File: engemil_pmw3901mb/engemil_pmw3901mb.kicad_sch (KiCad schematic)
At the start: 18 parts, among them J1 6130XX11121, U1 PMW3901MB-TXQT, U2 TLV77333PDBVR, U3 TLV77318PDBVR

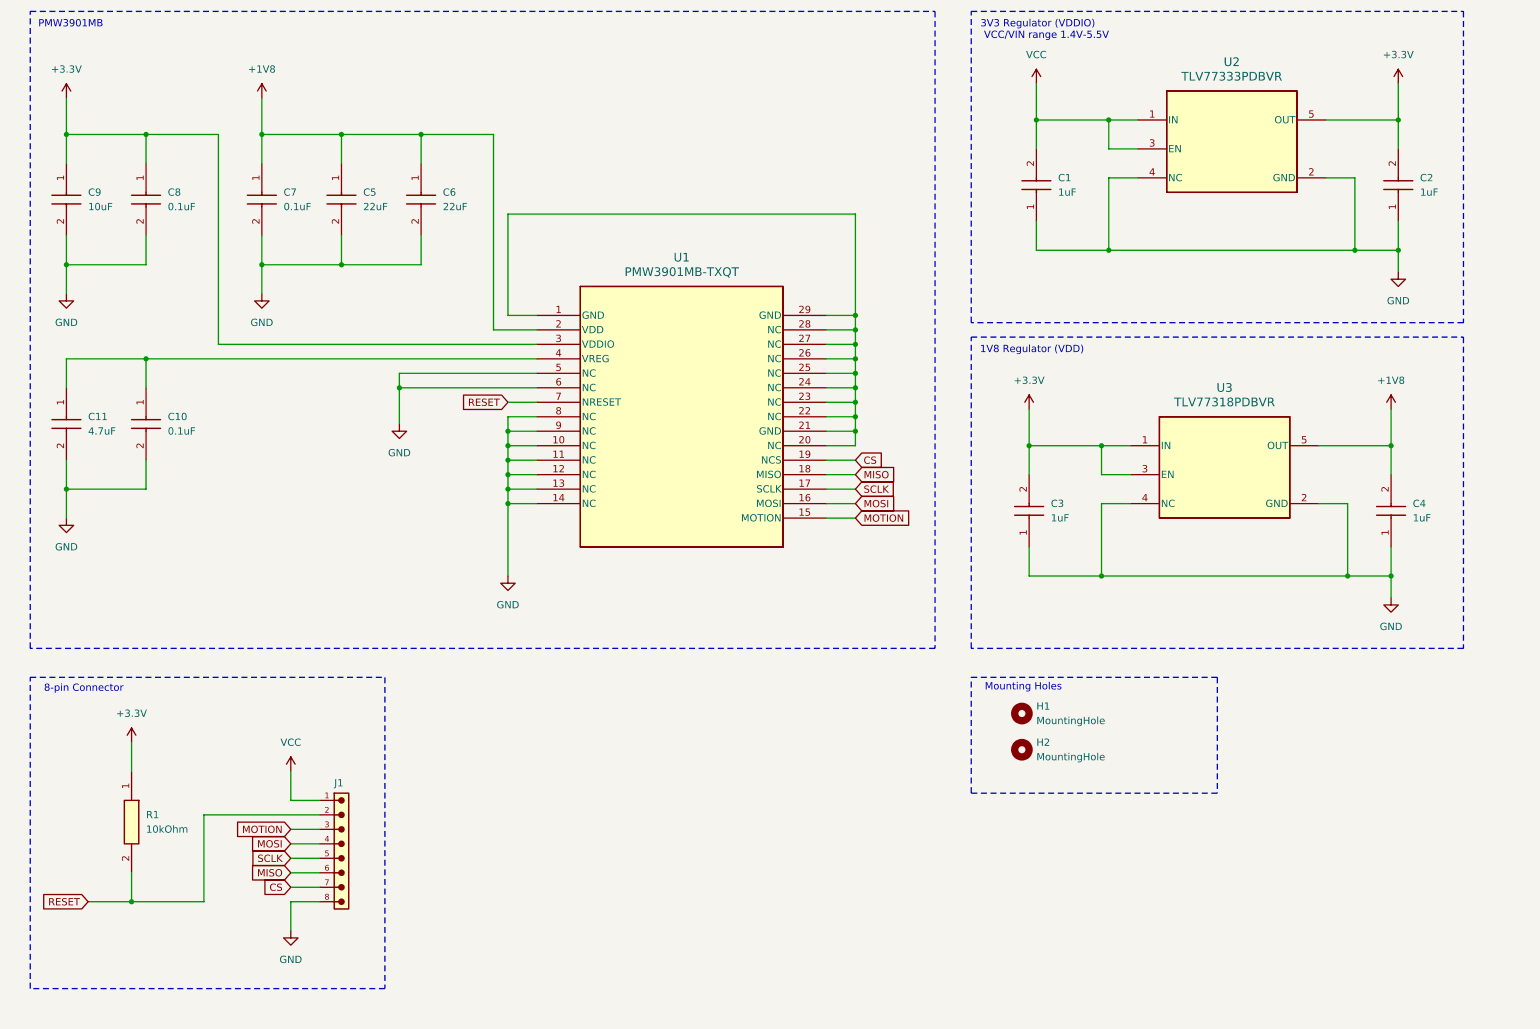
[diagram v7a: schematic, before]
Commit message: - Removed 3v3 voltage regulator and two capacitors - Changed reference designators (C1,C2,...,U2,U3,...) - Added R4 - Marked C3 and C4 as not mount - Added comment about RC filter - Added pull-up resistors for SCLK and MISO - Marked R2 and R3 as not mount - Added notes for 8-pin connector - Added ESD protection diodes - Updated BOM - Removed zip file in raw folder (unused and not imported) - Added datasheets for components under docs folder - Imported new components into project - Updated schematic version and date - Generated new schematic pdf - Started on redesigning pcb layout (work-in-progress)
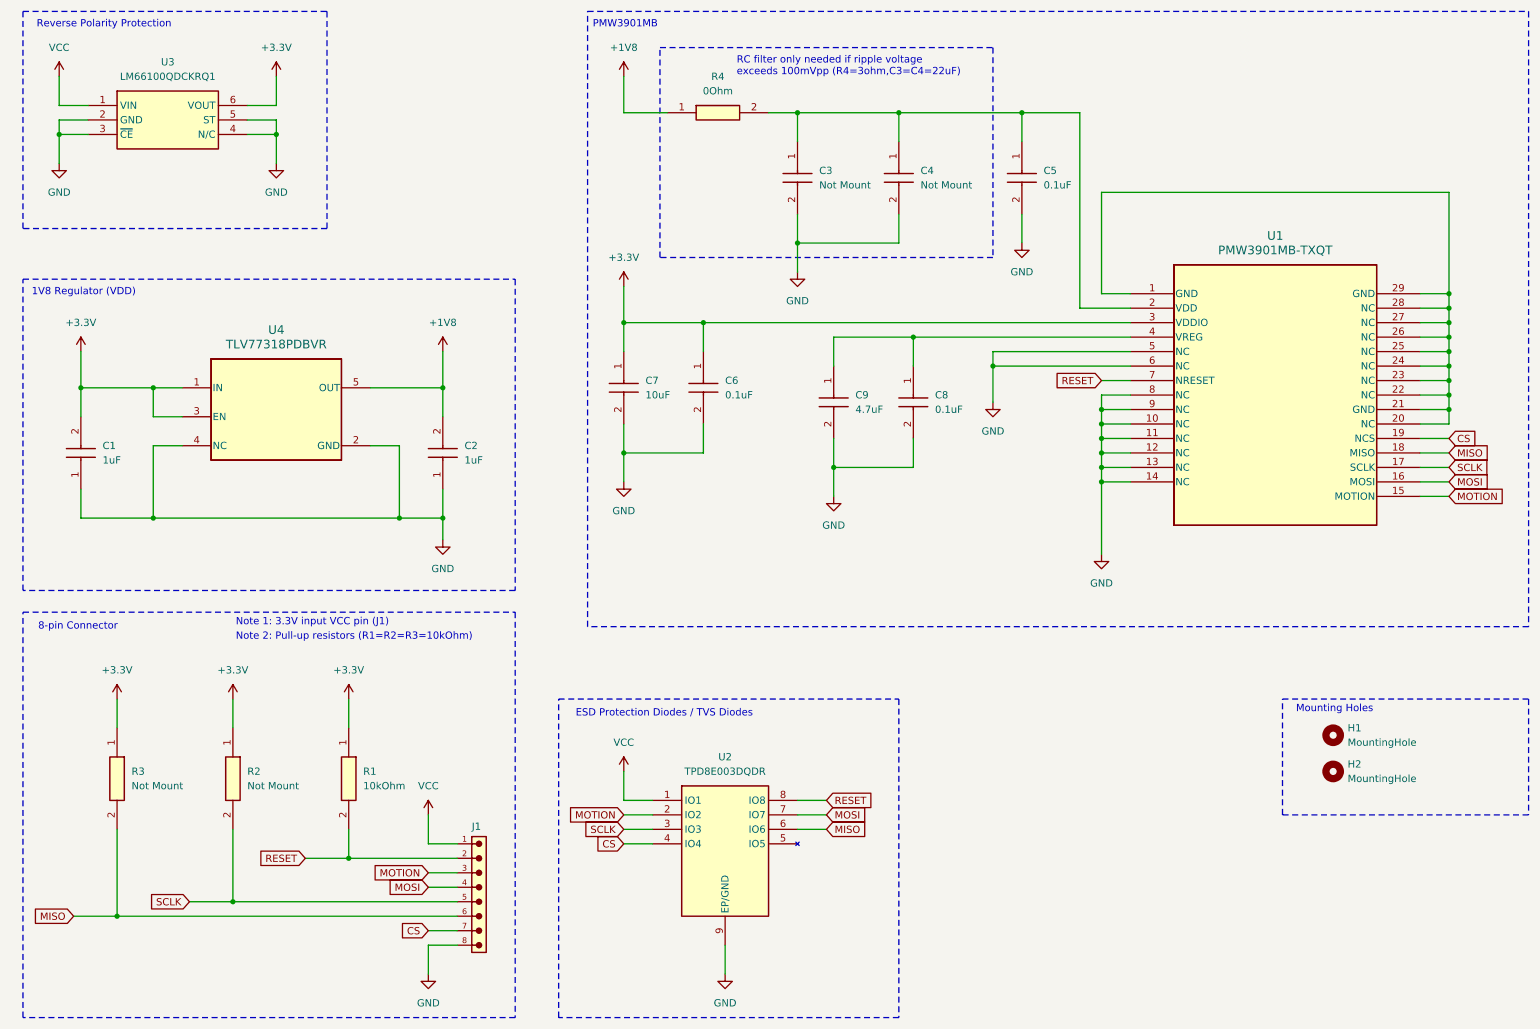
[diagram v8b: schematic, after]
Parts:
- removed C1, C2: 1uF, engemil_pmw3901mb_module_footprint_library:C0805, symbol engemil_pmw3901mb_module_symbol_library:C0805C105J4RECAUTO7210
- removed U2: TLV77333PDBVR, DBV0005A-IPC_A, symbol engemil_pmw3901mb_module_symbol_library:TLV77333PDBVR
- added R2, R3: Not Mount, RESC2012X60N, symbol engemil_pmw3901mb_module_symbol_library:RE0805FRE0710KL
- added R4: 0Ohm, engemil_pmw3901mb_module_footprint_library:RESC2012X60N, symbol engemil_pmw3901mb_module_symbol_library:RC0805FR-100RL
- added U2: TPD8E003DQDR, engemil_pmw3901mb_module_footprint_library:SON40P135X170X80-9N, symbol engemil_pmw3901mb_module_symbol_library:TPD8E003DQDR
- added U3: LM66100QDCKRQ1, engemil_pmw3901mb_module_footprint_library:SOT65P210X110-6N, symbol engemil_pmw3901mb_module_symbol_library:LM66100QDCKRQ1
- C3: renamed from C5; value 22uF -> Not Mount
- C4: renamed from C6; value 22uF -> Not Mount
- renumbered C3 to C1, C4 to C2, C7 to C5, C8 to C6, C9 to C7, C10 to C8, C11 to C9, U3 to U4
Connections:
- net +1V8: now also R4.1; no longer C3.1, C4.1, C5.1, U1.2 (VDD)
- net +3.3V: now also R2.1, R3.1, U3.6 (VOUT)
- net CS: now also U2.4 (IO4)
- net GND: now also U2.9 (EP/GND), U3.2 (GND), U3.3 (~{CE}), U3.4 (N/C), U3.5 (ST)
- net MISO: now also R3.2, U2.6 (IO6)
- net MOSI: now also U2.7 (IO7)
- net MOTION: now also U2.2 (IO2)
- net RESET: now also U2.8 (IO8)
- net SCLK: now also R2.2, U2.3 (IO3)
- net VCC: now also U2.1 (IO1), U3.1 (VIN)
- new net: C3.1, C4.1, C5.1, R4.2, U1.2 (VDD)
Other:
- note added: "ESD Protection Diodes / TVS Diodes"
- note added: "Note 1: 3.3V input VCC pin (J1)"
- note added: "Note 2: Pull-up resistors (R1=R2=R3=10kOhm)"
- note added: "RC filter only needed if ripple voltage exceeds 100mVpp (R4=3ohm,C3=C4=22uF)"
- note added: "Reverse Polarity Protection"
- note removed: "3V3 Regulator (VDDIO)"
- note removed: "VCC/VIN range 1.4V-5.5V"
- moved on the sheet: C1, C2, C3, C4, C5, C6, C7, C8, C9, H1, H2, J1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
